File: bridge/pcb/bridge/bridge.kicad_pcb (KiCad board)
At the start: 4 copper layers, 108 x 80 mm, 42 parts, among them J1 Screw_Terminal_01x06, J2 Screw_Terminal_01x06, J3 Screw_Terminal_01x06, J4 Conn_01x23, J5 Conn_01x04, J6 Conn_01x02, J7 Conn_01x03, J8 Conn_01x02, J9 MCU_Test_Point, SW1 SW_SPST, U1 L293, U2 J104D2C12VDC.20S, U3 AD557JN, U4 ATmega328P-P, U5 L7805

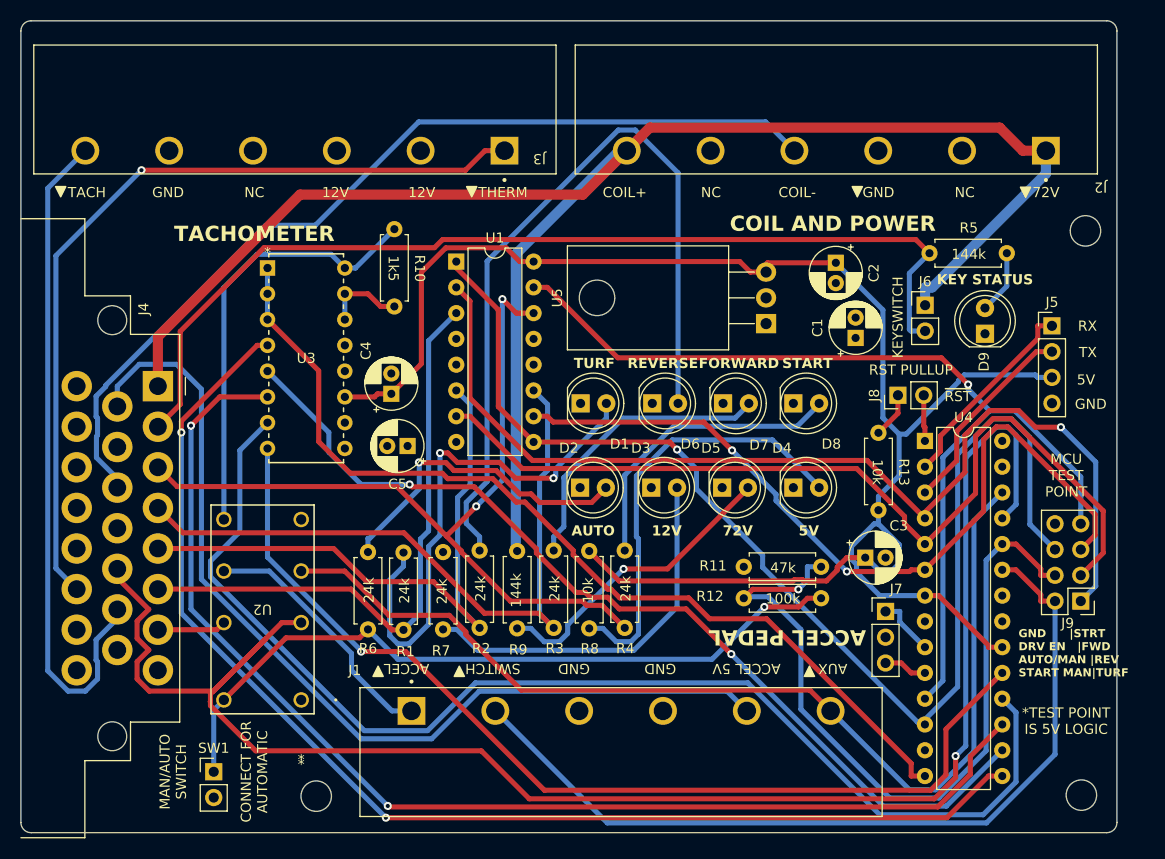
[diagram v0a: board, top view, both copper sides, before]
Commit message: Changed PCB back to 2 layer
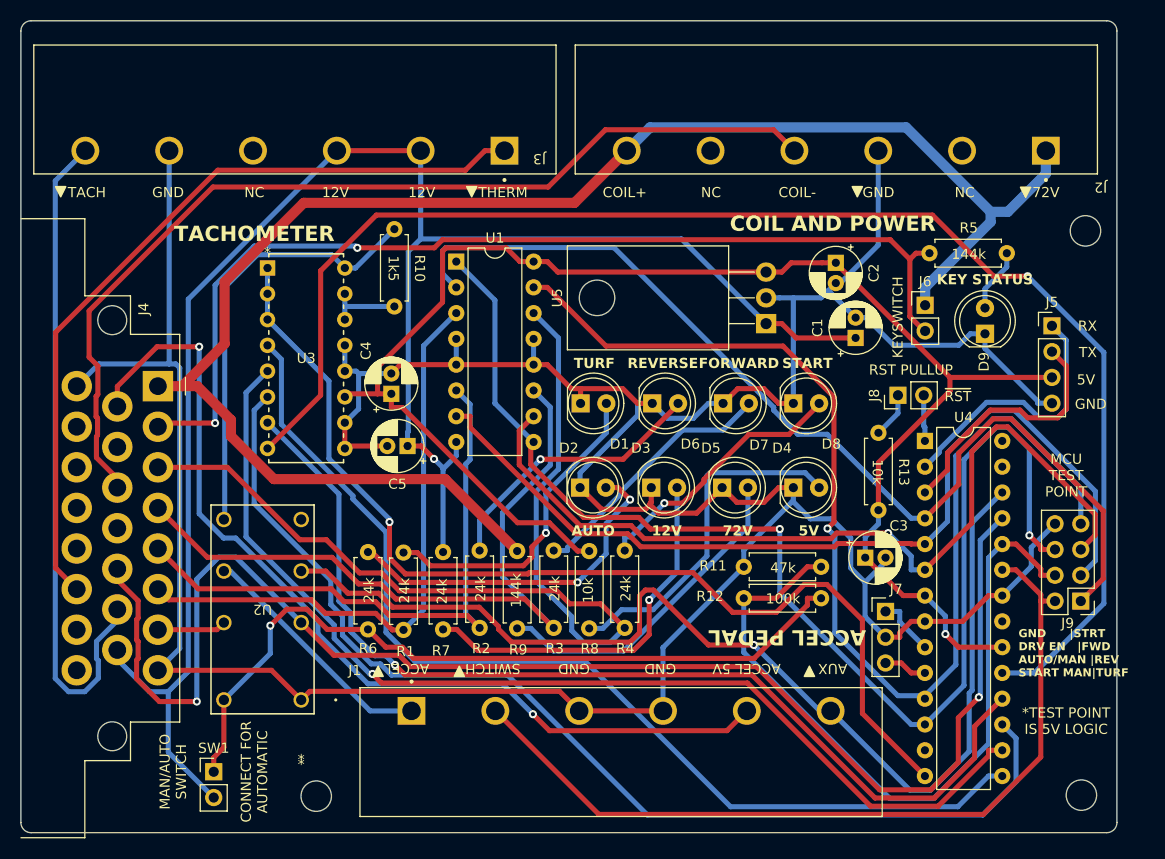
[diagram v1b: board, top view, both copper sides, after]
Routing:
- net GND: track 0.00 -> 356.5 mm
- net +12V: track 0.00 -> 180.4 mm, vias 0 -> 1
- net Net-(D6-A): track 78.5 -> 27.4 mm, vias 0 -> 1
- net Net-(U3-(MSB)BIT1): track 100.1 -> 142.3 mm
- net ACCEL_POT_AUX: track 167.2 -> 143.2 mm, vias 1 -> 2
- net Net-(D1-A): track 52.8 -> 31.7 mm, vias 2 -> 1
- net Net-(U3-BIT2): track 120.6 -> 100.9 mm, vias 0 -> 1
- net Net-(U3-BIT5): track 121.5 -> 102.2 mm, vias 2 -> 0
- net +5V: track 171.2 -> 153.8 mm, vias 0 -> 1
- net MCU_START: track 97.6 -> 114.6 mm
- net Net-(U3-BIT4): track 93.8 -> 106.1 mm, vias 2 -> 1
- net START_SWITCH: track 81.9 -> 93.5 mm, vias 2 -> 0
- net Net-(U3-BIT3): track 119.2 -> 108.9 mm, vias 2 -> 0
- net Net-(U3-(LSB)BIT8): track 93.6 -> 103.0 mm, vias 0 -> 1
- net /5V_LED_A: track 42.9 -> 34.3 mm
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- removed copper zone on In2.Cu, net +12V
- removed copper zone on In1.Cu, net GND
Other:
- copper layers 4 -> 2

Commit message: Assigned footprints and added new components to PCB
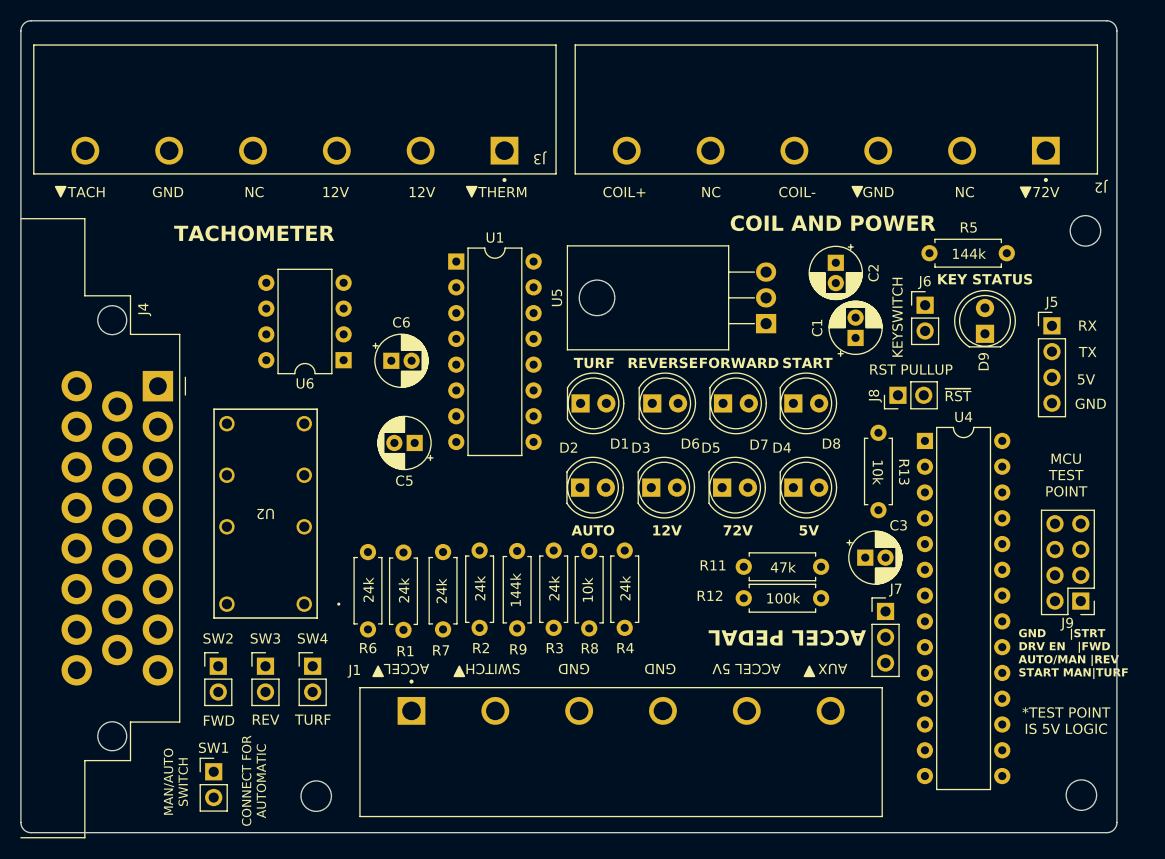
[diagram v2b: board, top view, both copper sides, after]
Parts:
- removed C4: 1u, Capacitor_THT:CP_Radial_D5.0mm_P2.00mm
- removed R10: 1k5, bridge:THT_RESISTOR_WITH_VALUE
- removed U3: AD557JN, bridge:AD557JN
- added C6: 1u, Capacitor_THT:CP_Radial_D5.0mm_P2.00mm, F.Cu at (99.5, 74.5)
- added SW2: SW_SPST, Connector_PinHeader_2.54mm:PinHeader_1x02_P2.54mm_Vertical, F.Cu at (82.5, 104.6)
- added SW3: SW_SPST, Connector_PinHeader_2.54mm:PinHeader_1x02_P2.54mm_Vertical, F.Cu at (87.1, 104.6)
- added SW4: SW_SPST, Connector_PinHeader_2.54mm:PinHeader_1x02_P2.54mm_Vertical, F.Cu at (91.8, 104.6)
- added U6: MCP4901, Package_DIP:DIP-8_W7.62mm, F.Cu at (94.8, 74.4)
- moved U2 9.44 mm to (90.9, 98.5)
- moved C5 0.76 mm to (101.8, 82.6)
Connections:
- J5 pad 3: +5V -> GND
- J5 pad 4: GND -> +5V
- U4 pad 13: unconnected-(U4-PD7-Pad13) -> LDAC
- U4 pad 14: Net-(U3-(LSB)BIT8) -> FORWARD_MAN
- U4 pad 15: Net-(U3-BIT5) -> REVERSE_MAN
- U4 pad 16: Net-(U3-BIT4) -> DAC_SS
- U4 pad 17: Net-(U3-BIT3) -> SPI_MOSI
- U4 pad 18: Net-(U3-BIT2) -> TURF_MAN
- U4 pad 19: Net-(U3-(MSB)BIT1) -> SPI_SCK
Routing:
- net GND: track 356.5 -> 0.00 mm
- net +12V: track 180.4 -> 0.00 mm, vias 1 -> 0
- net +BATT: track 161.5 -> 0.00 mm
- net +5V: track 153.8 -> 0.00 mm, vias 1 -> 0
- net ACCEL_POT_AUX: track 143.2 -> 0.00 mm, vias 2 -> 0
- net Net-(U3-(MSB)BIT1): track 142.3 -> 0.00 mm, vias 1 -> 0
- net DRV_ENABLE: track 124.6 -> 0.00 mm, vias 2 -> 0
- net MCU_START: track 114.6 -> 0.00 mm, vias 1 -> 0
- net ACCEL_AUX_MAN: track 109.7 -> 0.00 mm, vias 1 -> 0
- net Net-(U3-BIT3): track 108.9 -> 0.00 mm
- net Net-(U3-BIT4): track 106.1 -> 0.00 mm, vias 1 -> 0
- net Net-(U3-(LSB)BIT8): track 103.0 -> 0.00 mm, vias 1 -> 0
- net Net-(U3-BIT5): track 102.2 -> 0.00 mm
- net Net-(U3-BIT2): track 100.9 -> 0.00 mm, vias 1 -> 0
- net KEYSWITCH: track 100.6 -> 0.00 mm, vias 2 -> 0
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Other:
- board text added: "FWD"
- board text added: "REV"

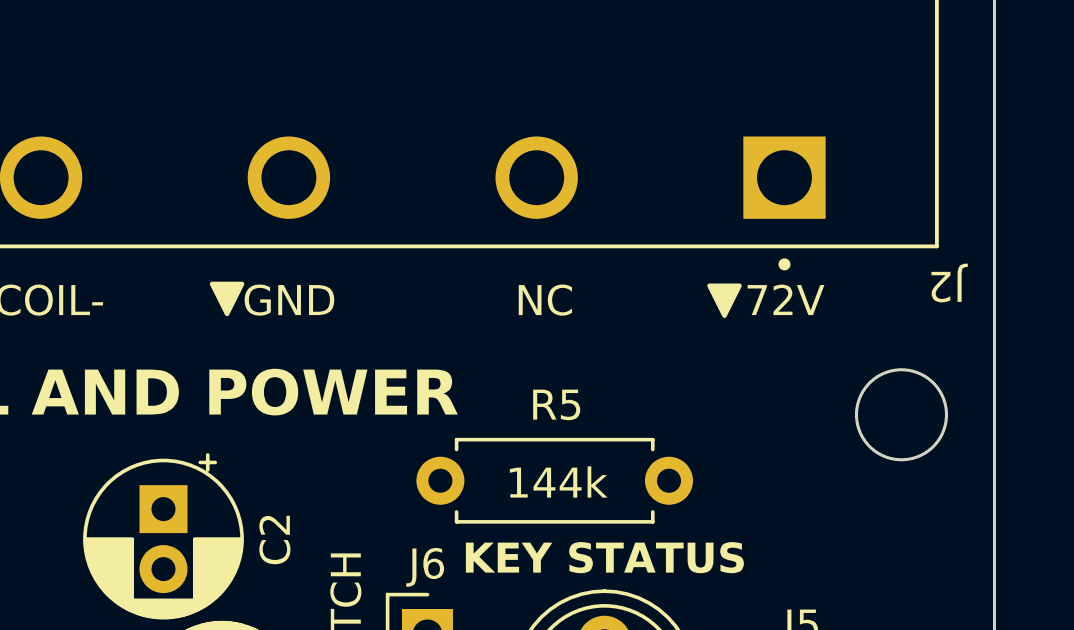
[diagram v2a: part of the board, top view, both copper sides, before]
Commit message: Added clarification to silkscreen for main power input connections
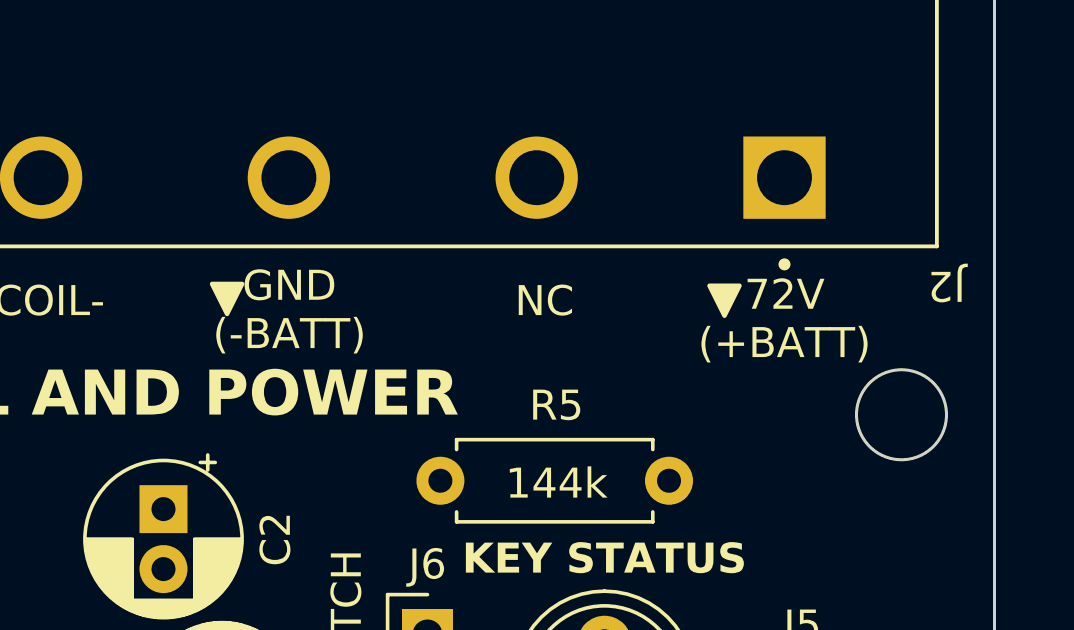
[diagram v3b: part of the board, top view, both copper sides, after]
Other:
- board text added: "72V (+BATT)"
- board text added: "GND (-BATT)"
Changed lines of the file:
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@@
     (effects (font (size 1 1) (thickness 0.15)) (justify bottom))
   )
-  (gr_text "GND" (at 147.5 58.5) (layer "F.SilkS")
+  (gr_text "GND\n(-BATT)" (at 147.5 59.6) (layer "F.SilkS")
     (effects (font (size 1 1) (thickness 0.15)) (justify bottom))
   )
@@
     (effects (font (size 1 1) (thickness 0.2) bold))
   )
-  (gr_text "72V" (at 164 58.5) (layer "F.SilkS")
+  (gr_text "72V\n(+BATT)" (at 164 59.9) (layer "F.SilkS")
     (effects (font (size 1 1) (thickness 0.15)) (justify bottom))
   )

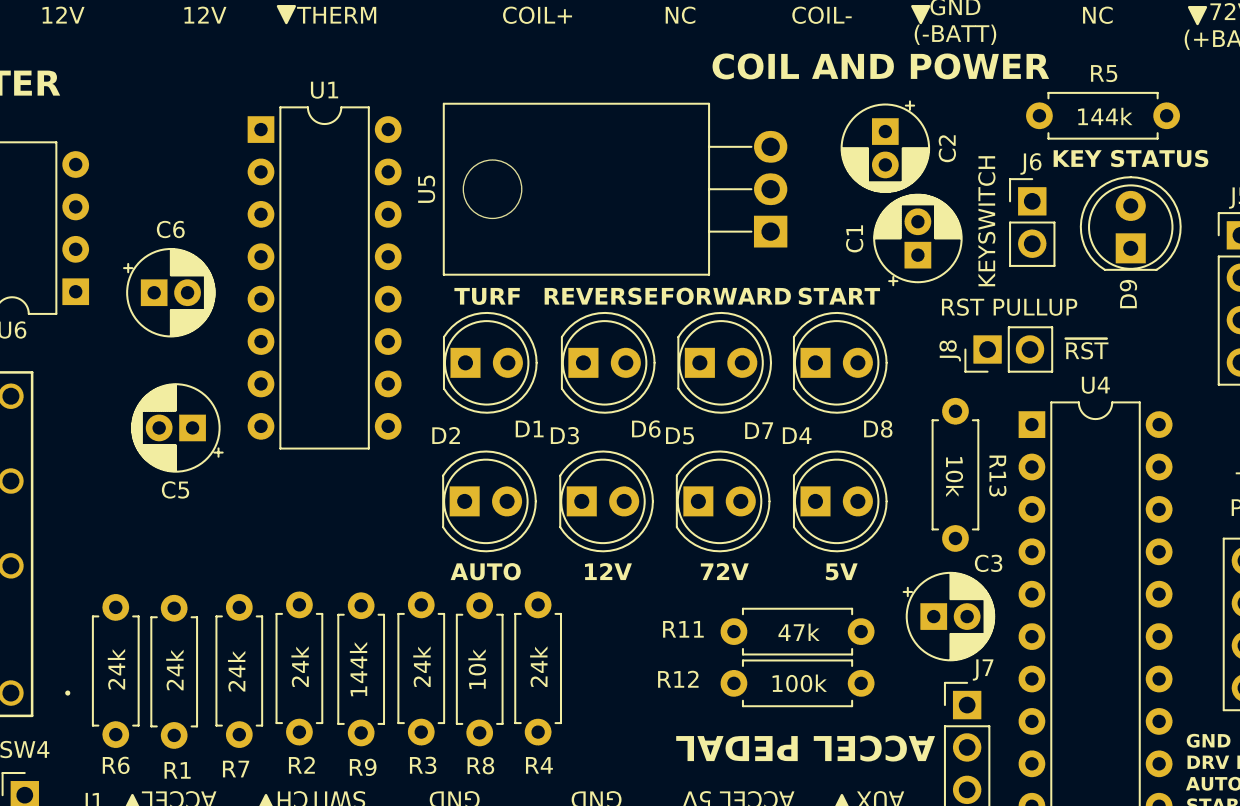
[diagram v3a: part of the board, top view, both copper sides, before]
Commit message: Updated resistor values to make LEDs brighter
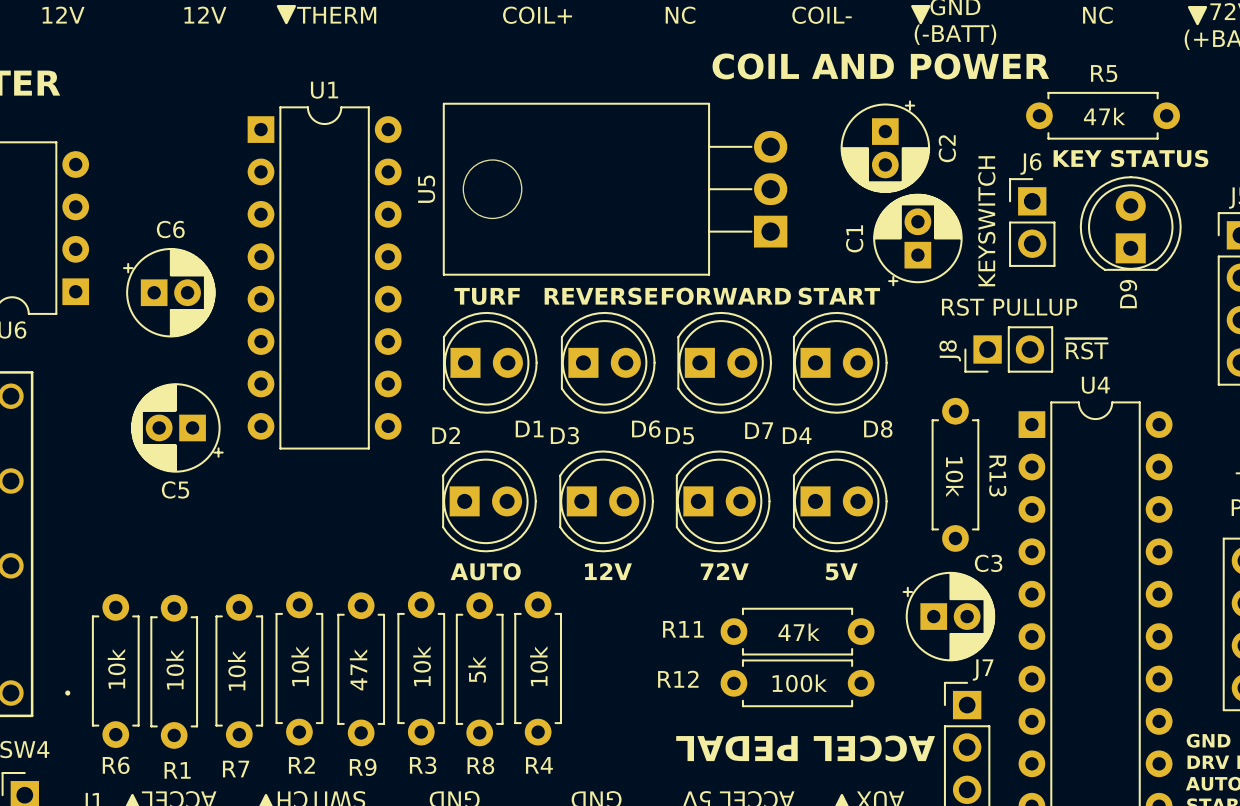
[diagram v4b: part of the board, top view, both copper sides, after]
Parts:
- R1, R2, R3, R4, R6, R7: value 24k -> 10k
- R5, R9: value 144k -> 47k
- R8: value 10k -> 5k
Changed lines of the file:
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@@
         (effects (font (size 1 1) (thickness 0.1)))
     )
-    (fp_text value "24k" (at 0 0 90 unlocked) (layer "F.SilkS")
+    (fp_text value "10k" (at 0 0 90 unlocked) (layer "F.SilkS")
         (effects (font (size 1 1) (thickness 0.15)))
     )
@@
         (effects (font (size 1 1) (thickness 0.1)))
     )
-    (fp_text value "24k" (at 0 0 90 unlocked) (layer "F.SilkS")
+    (fp_text value "10k" (at 0 0 90 unlocked) (layer "F.SilkS")
         (effects (font (size 1 1) (thickness 0.15)))
     )
@@
         (effects (font (size 1 1) (thickness 0.1)))
     )
-    (fp_text value "24k" (at 0 0 90 unlocked) (layer "F.SilkS")
+    (fp_text value "10k" (at 0 0 90 unlocked) (layer "F.SilkS")
         (effects (font (size 1 1) (thickness 0.15)))
     )
@@
         (effects (font (size 1 1) (thickness 0.1)))
     )
-    (fp_text value "24k" (at 0 0 90 unlocked) (layer "F.SilkS")
+    (fp_text value "10k" (at 0 0 90 unlocked) (layer "F.SilkS")
         (effects (font (size 1 1) (thickness 0.15)))
     )
@@
         (effects (font (size 1 1) (thickness 0.1)))
     )
-    (fp_text value "24k" (at 0 0 90 unlocked) (layer "F.SilkS")
+    (fp_text value "10k" (at 0 0 90 unlocked) (layer "F.SilkS")
         (effects (font (size 1 1) (thickness 0.15)))
     )
@@
         (effects (font (size 1 1) (thickness 0.1)))
     )
-    (fp_text value "24k" (at 0 0 90 unlocked) (layer "F.SilkS")
+    (fp_text value "10k" (at 0 0 90 unlocked) (layer "F.SilkS")
         (effects (font (size 1 1) (thickness 0.15)))
     )
@@
         (effects (font (size 1 1) (thickness 0.1)))
     )
-    (fp_text value "144k" (at 0 0 unlocked) (layer "F.SilkS")
+    (fp_text value "47k" (at 0 0 unlocked) (layer "F.SilkS")
         (effects (font (size 1 1) (thickness 0.15)))
     )
@@
         (effects (font (size 1 1) (thickness 0.1)))
     )
-    (fp_text value "10k" (at 0 0 90 unlocked) (layer "F.SilkS")
+    (fp_text value "5k" (at 0 0 90 unlocked) (layer "F.SilkS")
         (effects (font (size 1 1) (thickness 0.15)))
     )
@@
         (effects (font (size 1 1) (thickness 0.1)))
     )
-    (fp_text value "144k" (at 0 0 90 unlocked) (layer "F.SilkS")
+    (fp_text value "47k" (at 0 0 90 unlocked) (layer "F.SilkS")
         (effects (font (size 1 1) (thickness 0.15)))
     )
